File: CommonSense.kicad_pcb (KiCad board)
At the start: 2 copper layers, 34 x 24 mm, 29 parts, among them J1 Conn_02x04_Counter_Clockwise, U1 NRF52810-QFAA-R7, U2 SHT41-AD1B-R2, Y1 ECS-.327-12.5-12R-TR, Y2 ABM11W-32.0000MHZ-7-D1X-T3

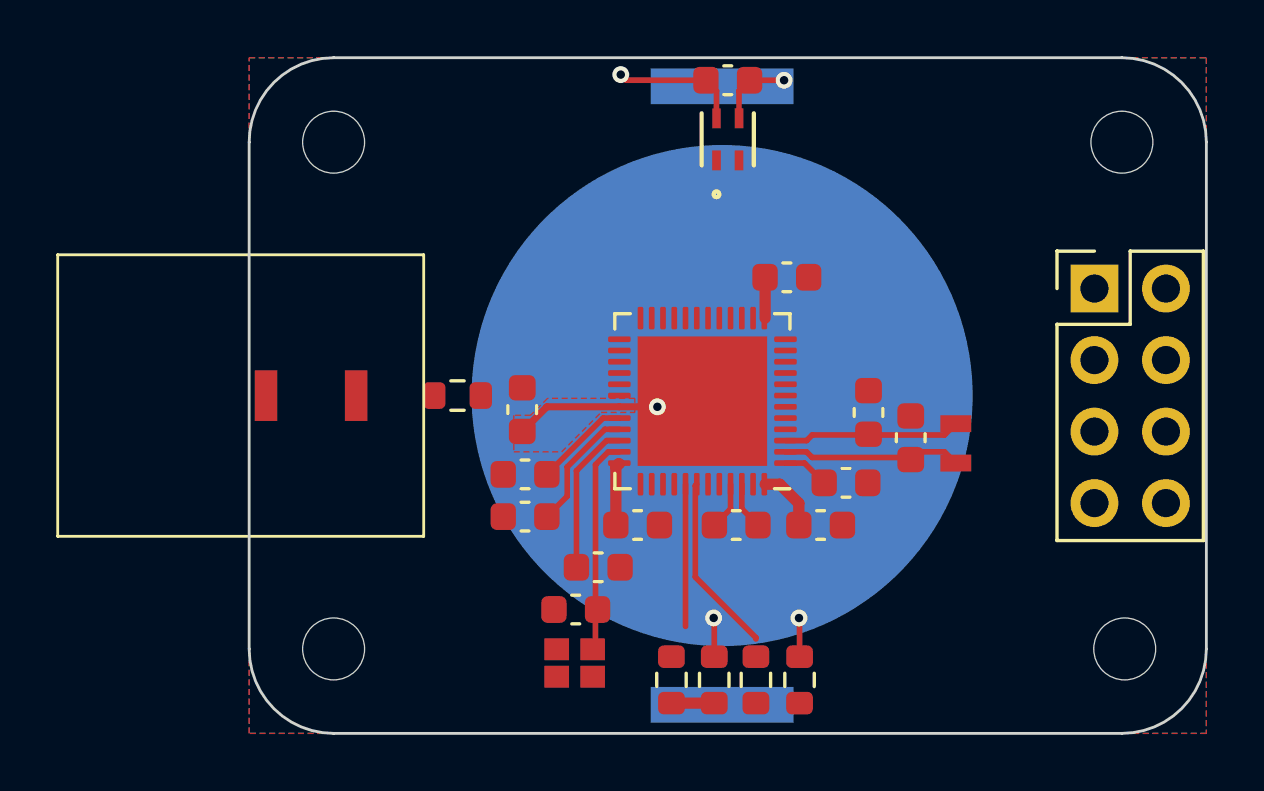
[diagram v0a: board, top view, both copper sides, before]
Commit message: Fix most DRC violations
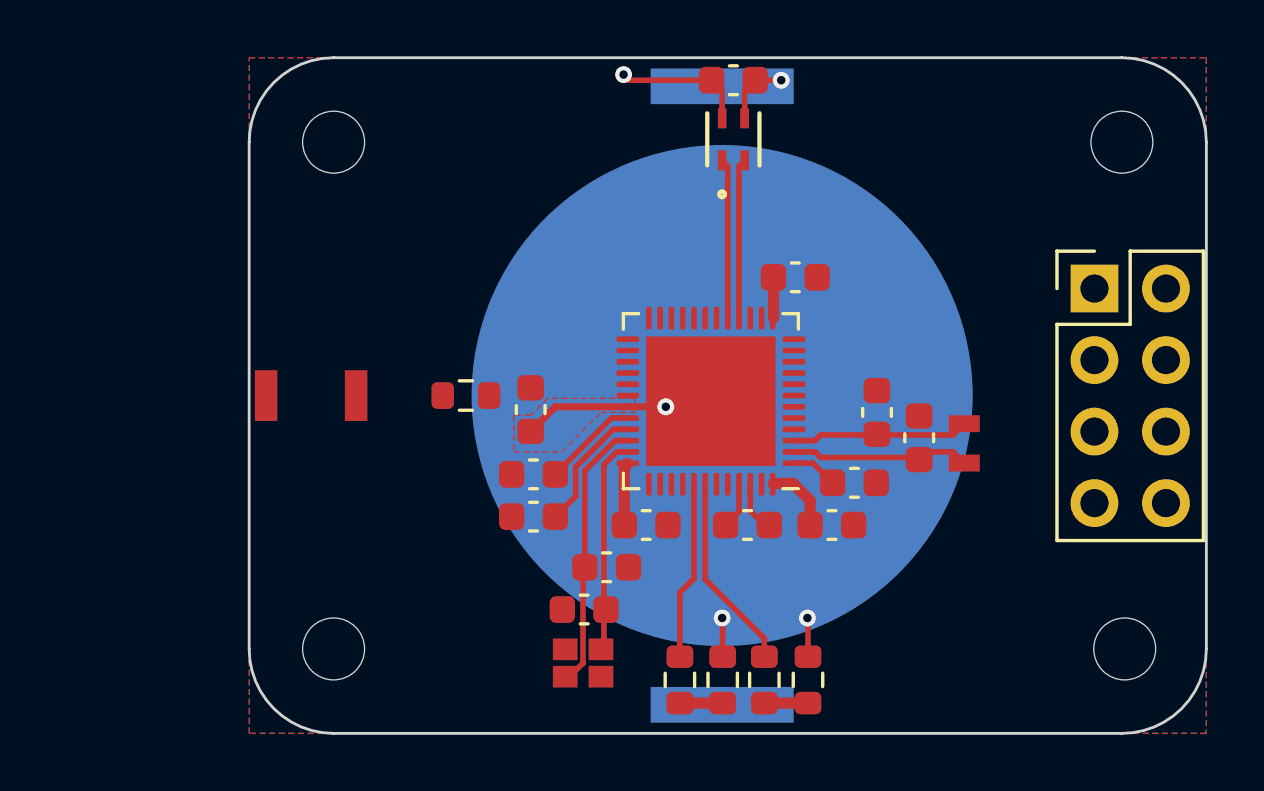
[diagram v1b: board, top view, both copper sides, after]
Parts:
- moved C5 0.40 mm to (156.7, 72.6)
- moved C6 0.40 mm to (153.7, 72.6)
- moved C1 0.30 mm to (159.8, 69.5)
- moved C10 0.30 mm to (147.9, 75.6)
- moved C12 0.30 mm to (146.0, 68.5)
- moved C2 0.30 mm to (158.3, 68.6)
- moved C3 0.30 mm to (157.5, 71.1)
- moved C4 0.30 mm to (155.4, 63.8)
- moved R1 0.30 mm to (154.3, 78.1)
- moved R2 0.30 mm to (151.3, 78.1)
- moved U1 0.30 mm to (152.4, 68.2)
- moved Y1 0.30 mm to (161.4, 69.7)
- moved Y2 0.30 mm to (147.9, 77.5)
- moved C11 0.30 mm to (148.7, 74.1)
- moved C7 0.30 mm to (150.1, 72.6)
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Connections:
- U1 pad 16: unconnected-(U1-P0.13-Pad16) -> /SCL
- U1 pad 17: unconnected-(U1-P0.14-Pad17) -> /SDA
- U1 pad 41: unconnected-(U1-P0.29/AIN5-Pad41) -> /STATUS_LED2
- U1 pad 42: unconnected-(U1-P0.30/AIN6-Pad42) -> /STATUS_LED1
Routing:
- net /STATUS_LED1: track 0.00 -> 6.99 mm
- net unconnected-(U1-P0.30/AIN6-Pad42): track 6.41 -> 0.00 mm
- net /STATUS_LED2: track 0.00 -> 6.33 mm
- net /SDA: track 0.00 -> 5.69 mm
- net /SCL: track 0.00 -> 5.69 mm
- net unconnected-(U1-P0.29/AIN5-Pad41): track 5.05 -> 0.00 mm
- net /XC2: track 5.40 -> 9.66 mm
- net /LED_RES1: track 0.00 -> 1.55 mm

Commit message: Routed all connections
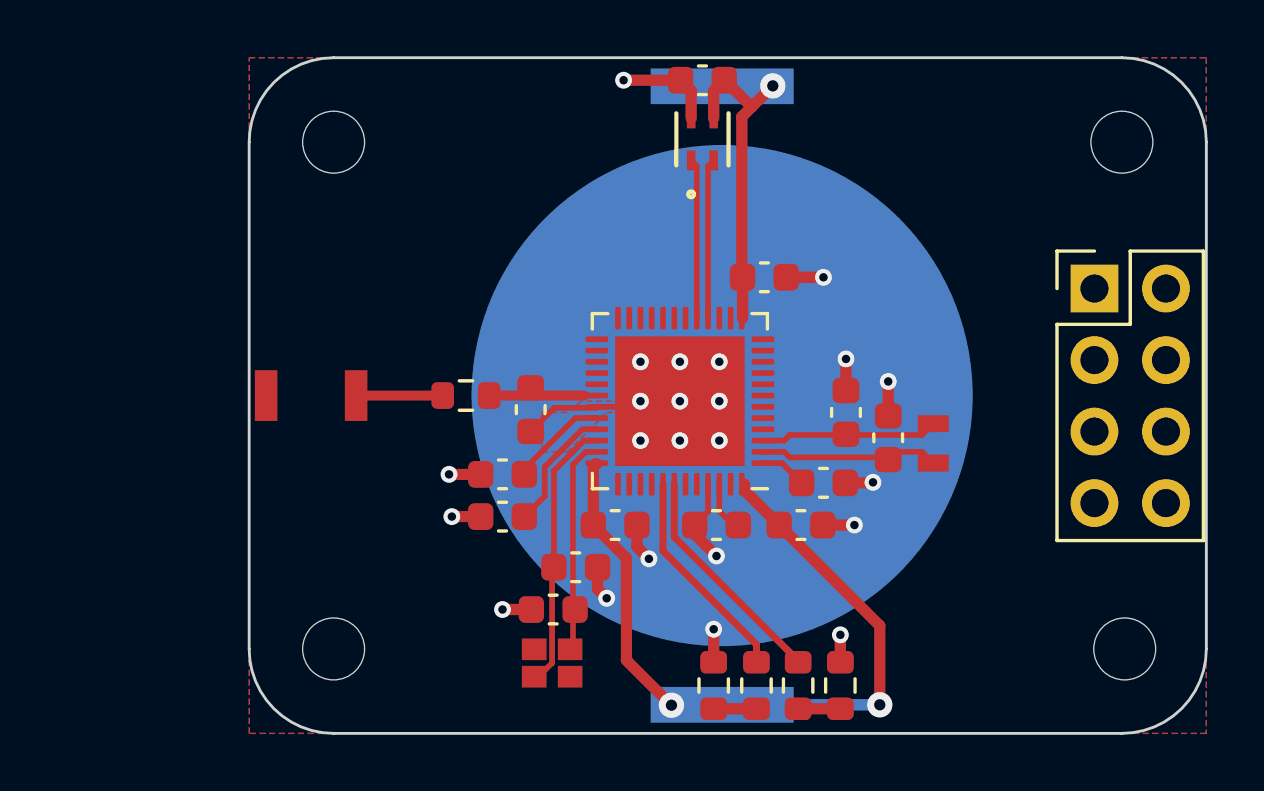
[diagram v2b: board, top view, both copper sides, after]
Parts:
- moved R2 2.73 mm to (154.0, 78.3)
- moved R1 1.22 mm to (155.5, 78.3)
- moved D1 1.17 mm to (157.0, 78.3)
- moved C1 1.10 mm to (158.7, 69.5)
- moved C2 1.10 mm to (157.2, 68.6)
- moved Y2 1.10 mm to (146.8, 77.5)
- moved C10 1.10 mm to (146.8, 75.6)
- moved C11 1.10 mm to (147.6, 74.1)
- moved C13 1.10 mm to (152.1, 56.8)
- moved C3 1.10 mm to (156.4, 71.1)
- moved C4 1.10 mm to (154.3, 63.8)
- moved C5 1.10 mm to (155.6, 72.6)
- moved C6 1.10 mm to (152.6, 72.6)
- moved C7 1.10 mm to (149.0, 72.6)
- moved C8 1.10 mm to (145.0, 72.3)
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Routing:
- net +3V3: track 8.57 -> 36.8 mm, vias 1 -> 3
- net GND: track 14.3 -> 24.7 mm, vias 4 -> 23
- net /ANT: track 0.00 -> 3.82 mm
- net /RF: track 0.00 -> 3.07 mm
- net /STATUS_LED2: track 6.33 -> 7.70 mm
- net /STATUS_LED1: track 6.99 -> 8.15 mm

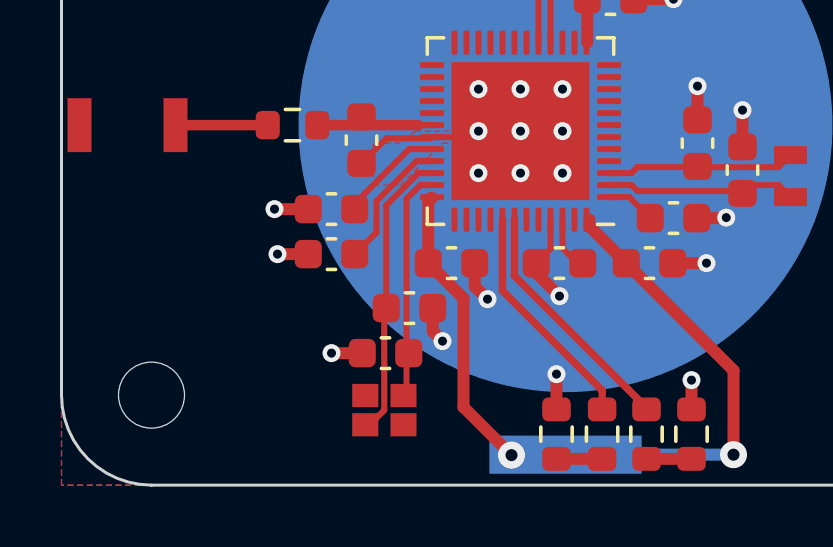
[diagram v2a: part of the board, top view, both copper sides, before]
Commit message: Minor cosmetic changes
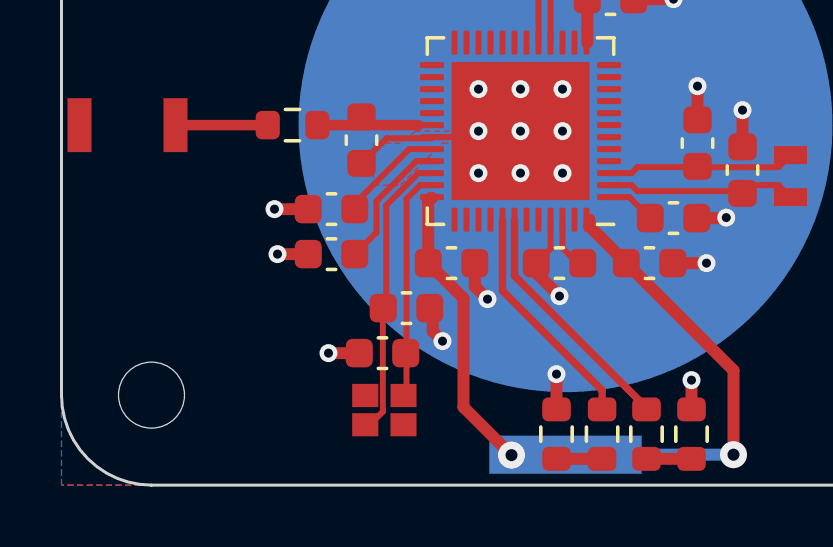
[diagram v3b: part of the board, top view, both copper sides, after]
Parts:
- moved C10 0.10 mm to (146.7, 75.6)
- moved C11 0.10 mm to (147.5, 74.1)
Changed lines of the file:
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@@
   )
   (footprint "Capacitor_SMD:C_0603_1608Metric" (layer "F.Cu")
-    (at 147.6 74.1)
+    (at 147.5 74.1)
     (descr "Capacitor SMD 0603 (1608 Metric), square (rectangular) end terminal, IPC_7351 nominal, (Body size source: IPC-SM-782 page 76, https://www.pcb-3d.com/wordpress/wp-content/uploads/ipc-sm-782a_amendment_1_and_2.pdf), generated with kicad-footprint-generator")
     (tags "capacitor")
@@
   )
   (footprint "Capacitor_SMD:C_0603_1608Metric" (layer "F.Cu")
-    (at 146.8 75.6 180)
+    (at 146.7 75.6 180)
     (descr "Capacitor SMD 0603 (1608 Metric), square (rectangular) end terminal, IPC_7351 nominal, (Body size source: IPC-SM-782 page 76, https://www.pcb-3d.com/wordpress/wp-content/uploads/ipc-sm-782a_amendment_1_and_2.pdf), generated with kicad-footprint-generator")
     (tags "capacitor")
@@
   (segment (start 152.3 72.125) (end 151.825 72.6) (width 0.2) (layer "F.Cu") (net 3))
   (segment (start 151.825 72.925) (end 152.6 73.7) (width 0.4) (layer "F.Cu") (net 3))
-  (segment (start 146.025 75.6) (end 145 75.6) (width 0.4) (layer "F.Cu") (net 3))
+  (segment (start 145.925 75.6) (end 144.9 75.6) (width 0.4) (layer "F.Cu") (net 3))
   (segment (start 157.2 67.825) (end 157.2 66.7) (width 0.4) (layer "F.Cu") (net 3))
   (segment (start 148.375 74.1) (end 148.375 74.875) (width 0.4) (layer "F.Cu") (net 3))
@@
   (via (at 151.3 69.6) (size 0.6) (drill 0.3) (layers "F.Cu" "B.Cu") (net 3))
   (via (at 158.15864 71.08272) (size 0.6) (drill 0.3) (layers "F.Cu" "B.Cu") (net 3))
-  (via (at 145 75.6) (size 0.6) (drill 0.3) (layers "F.Cu" "B.Cu") (net 3))
+  (via (at 144.9 75.6) (size 0.6) (drill 0.3) (layers "F.Cu" "B.Cu") (net 3))
   (via (at 157 76.5) (size 0.6) (drill 0.3) (layers "F.Cu" "B.Cu") (net 3))
   (via (at 148.7 75.2) (size 0.6) (drill 0.3) (layers "F.Cu" "B.Cu") (net 3))
@@
   (segment (start 147.958263 70) (end 147.502 70.456263) (width 0.2) (layer "F.Cu") (net 10))
   (segment (start 148.35 70) (end 147.958263 70) (width 0.2) (layer "F.Cu") (net 10))
-  (segment (start 146.825 70.670815) (end 146.825 74.1) (width 0.2) (layer "F.Cu") (net 11))
-  (segment (start 146.76 74.165) (end 146.825 74.1) (width 0.2) (layer "F.Cu") (net 11))
-  (segment (start 146.2765 77.987) (end 146.76 77.5035) (width 0.2) (layer "F.Cu") (net 11))
+  (segment (start 146.825 70.670815) (end 146.825 74) (width 0.2) (layer "F.Cu") (net 11))
+  (segment (start 146.713 77.5505) (end 146.2765 77.987) (width 0.2) (layer "F.Cu") (net 11))
+  (segment (start 146.713 74.112) (end 146.713 77.5505) (width 0.2) (layer "F.Cu") (net 11))
   (segment (start 147.895815 69.6) (end 146.825 70.670815) (width 0.2) (layer "F.Cu") (net 11))
+  (segment (start 146.2765 77.987) (end 146.1255 77.987) (width 0.2) (layer "F.Cu") (net 11))
   (segment (start 148.35 69.6) (end 147.895815 69.6) (width 0.2) (layer "F.Cu") (net 11))
-  (segment (start 146.1255 77.987) (end 146.2765 77.987) (width 0.2) (layer "F.Cu") (net 11))
-  (segment (start 146.76 77.5035) (end 146.76 74.165) (width 0.2) (layer "F.Cu") (net 11))
+  (segment (start 146.825 74) (end 146.713 74.112) (width 0.2) (layer "F.Cu") (net 11))
   (segment (start 147.9 68) (end 144.525 68) (width 0.35) (layer "F.Cu") (net 12))
   (segment (start 148.35 68) (end 147.9 68) (width 0.2) (layer "F.Cu") (net 12))

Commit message: Add version text
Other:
- board text added: "CommonSense v1.0"
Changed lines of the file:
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@@
   (gr_line locked (start 136 77) (end 136 59)
     (stroke (width 0.1) (type default)) (layer "Edge.Cuts"))
+  (gr_text "CommonSense v1.0" (at 162.9 60.6 90) (layer "B.SilkS")
+    (effects (font (size 1 1) (thickness 0.15)) (justify left top mirror))
+  )
   (segment (start 142.875 68) (end 139.8 68) (width 0.35) (layer "F.Cu") (net 1))
   (segment (start 153.5 63.775) (end 153.5 58.1) (width 0.4) (layer "F.Cu") (net 2))

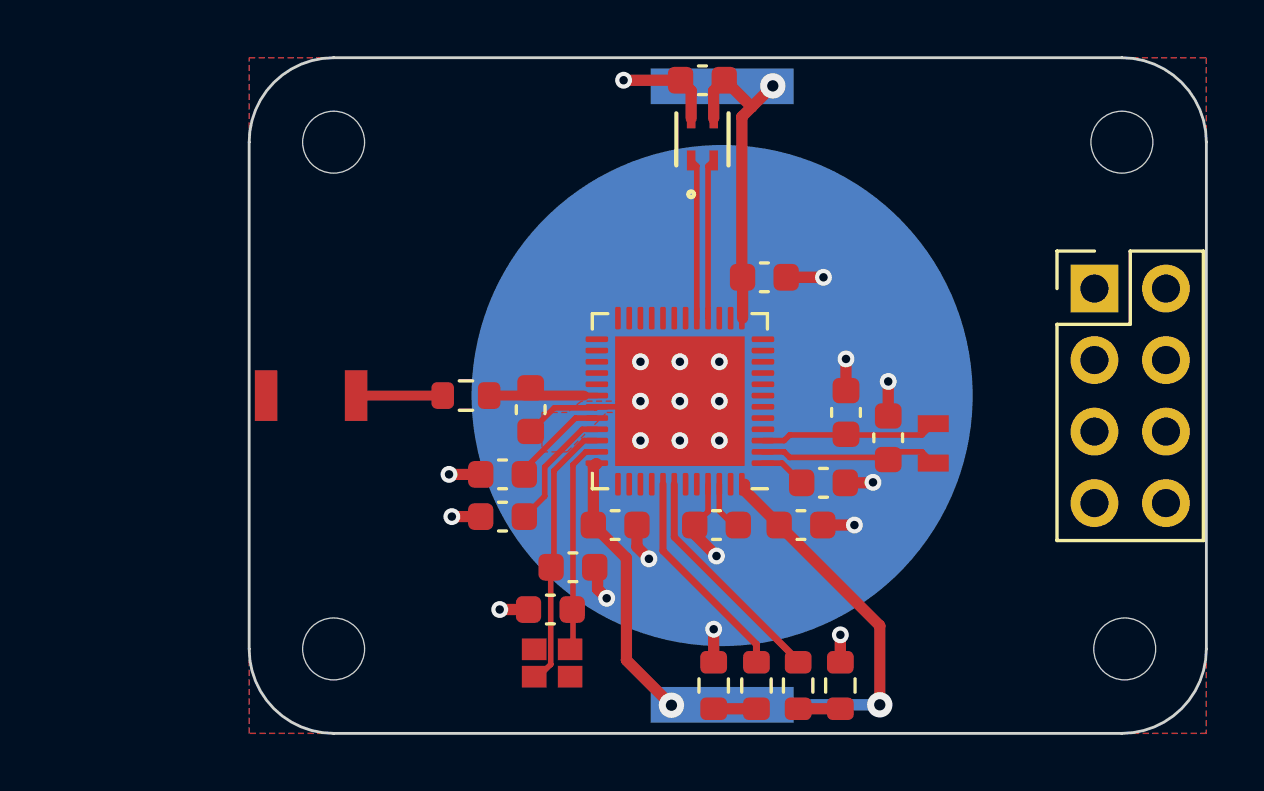
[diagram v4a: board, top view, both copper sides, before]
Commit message: Add I2C pullup resistors to PCB
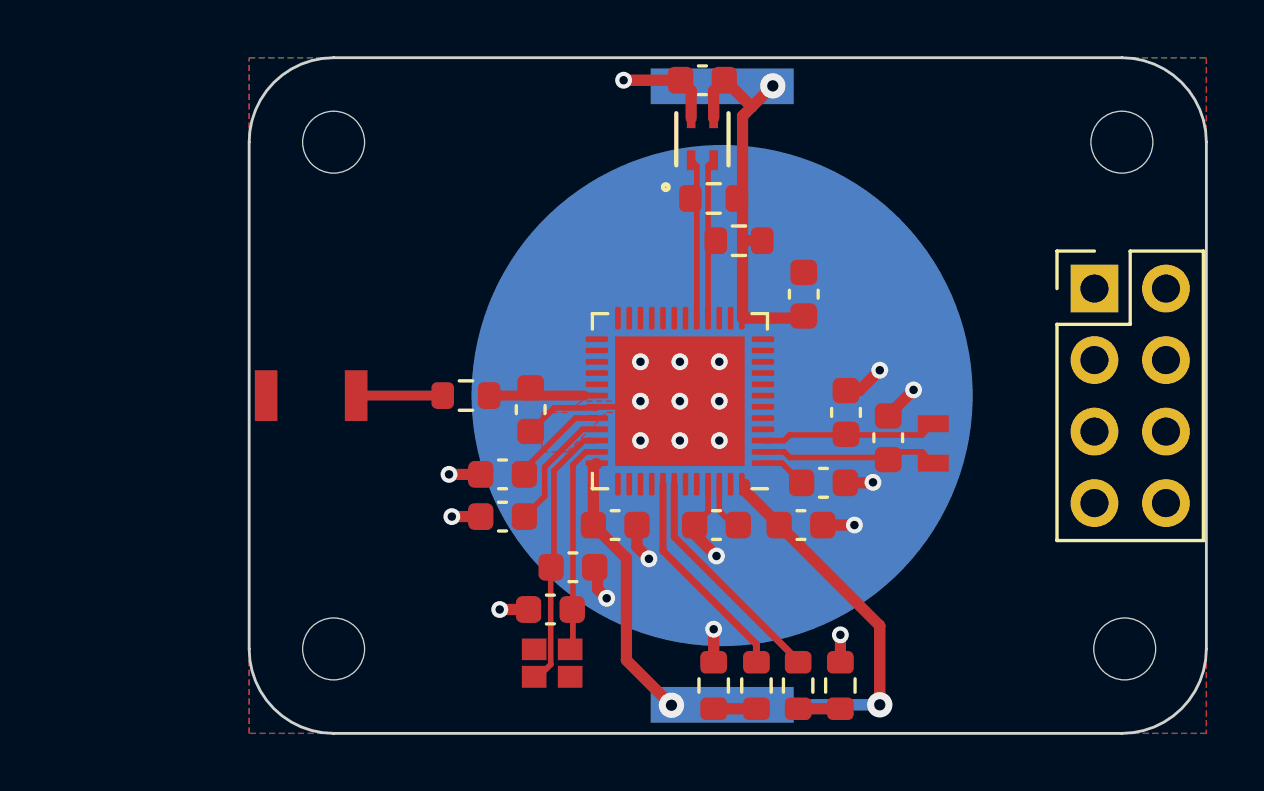
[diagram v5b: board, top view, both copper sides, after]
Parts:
- added R3: 10k, Resistor_SMD:R_0603_1608Metric, F.Cu at (153.4, 62.5)
- added R4: 10k, Resistor_SMD:R_0603_1608Metric, F.Cu at (152.5, 61.0)
- moved C4 1.52 mm to (155.7, 64.4), turned to -90 degrees
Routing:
- net +3V3: track 36.8 -> 39.7 mm
- net GND: track 24.7 -> 23.8 mm, vias 23 -> 22

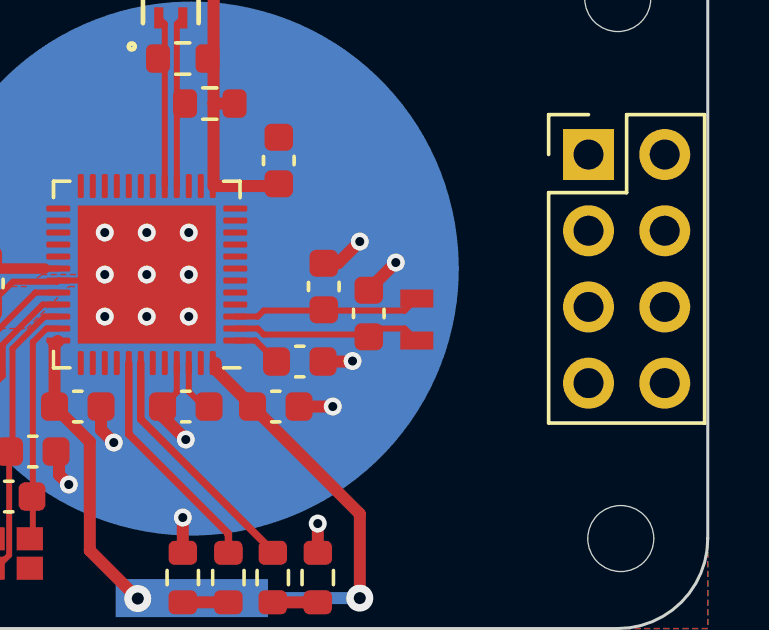
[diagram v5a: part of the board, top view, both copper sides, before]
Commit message: Start routing connections to pin header
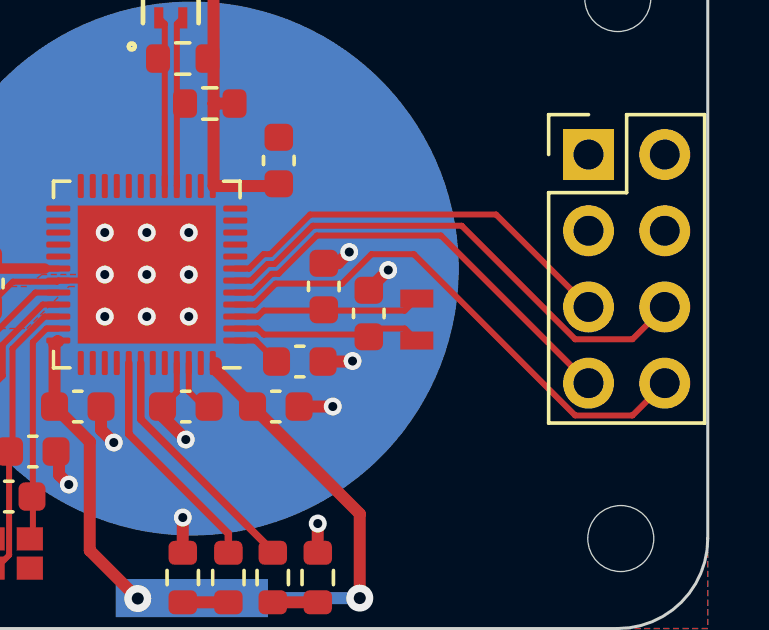
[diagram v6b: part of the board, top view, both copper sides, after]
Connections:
- J1 pad 1: unconnected-(J1-Pin_1-Pad1) -> /P0.09
- J1 pad 2: unconnected-(J1-Pin_2-Pad2) -> /P0.08
- J1 pad 3: unconnected-(J1-Pin_3-Pad3) -> /P0.07
- J1 pad 4: unconnected-(J1-Pin_4-Pad4) -> /P0.06
- J1 pad 5: unconnected-(J1-Pin_5-Pad5) -> /AIN3
- J1 pad 6: unconnected-(J1-Pin_6-Pad6) -> /AIN2
- J1 pad 7: unconnected-(J1-Pin_7-Pad7) -> /AIN1
- J1 pad 8: unconnected-(J1-Pin_8-Pad8) -> /AIN0
- U1 pad 10: unconnected-(U1-P0.08-Pad10) -> /P0.08
- U1 pad 11: unconnected-(U1-P0.09-Pad11) -> /P0.09
- U1 pad 4: unconnected-(U1-P0.02/AIN0-Pad4) -> /AIN0
- U1 pad 5: unconnected-(U1-P0.03/AIN1-Pad5) -> /AIN1
- U1 pad 6: unconnected-(U1-P0.04/AIN2-Pad6) -> /AIN2
- U1 pad 7: unconnected-(U1-P0.05/AIN3-Pad7) -> /AIN3
- U1 pad 8: unconnected-(U1-P0.06-Pad8) -> /P0.06
- U1 pad 9: unconnected-(U1-P0.07-Pad9) -> /P0.07
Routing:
- net /AIN0: track 0.00 -> 17.7 mm
- net /AIN2: track 0.00 -> 17.1 mm
- net /AIN1: track 0.00 -> 14.6 mm
- net /AIN3: track 0.00 -> 13.8 mm
- net GND: track 23.8 -> 22.9 mm
